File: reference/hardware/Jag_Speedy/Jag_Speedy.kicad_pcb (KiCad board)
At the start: 2 copper layers, 163 parts, among them IC1 MPX4250AP, IC10 SP720APP, IC11 VNS3NV04DP-E, IC12 SP720APP, IC2 MPX4250AP, IC3 VNS3NV04DP-E, IC4 VNS3NV04DP-E, IC5 VNS3NV04DP-E, IC6 TC4424EPA, IC7 TC4424EPA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

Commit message: Connector update
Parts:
- removed J3: Outputs02, Connector_PinHeader_1.00mm:PinHeader_2x05_P1.00mm_Horizontal
- removed J4: Power, Connector_PinHeader_1.00mm:PinHeader_1x05_P1.00mm_Horizontal
- removed J5: Bluetooth, Connector_PinHeader_1.00mm:PinHeader_1x06_P1.00mm_Horizontal
- removed J7: Canbus, Connector_PinHeader_1.00mm:PinHeader_1x06_P1.00mm_Horizontal
- J1: value Inputs -> 776087-1; footprint Connector_PinHeader_1.00mm:PinHeader_2x12_P1.00mm_Horizontal -> 776087-1:7760871
- J2: value Ouputs01 -> 776163-1; footprint Connector_PinHeader_1.00mm:PinHeader_2x07_P1.00mm_Horizontal -> 776163-1:776163-1
- moved J2 241.3 mm to (262.9, 161.3), turned to 90 degrees
- moved C23 157.9 mm to (245.1, 109.2)
- moved C24 157.9 mm to (244.8, 113.0)
- moved C25 157.9 mm to (244.8, 104.1)
- moved C26 157.9 mm to (244.8, 96.5)
- moved C27 157.9 mm to (244.8, 100.3)
- moved C28 157.9 mm to (244.8, 91.4)
- moved D1 157.9 mm to (241.0, 64.8)
- moved D10 157.9 mm to (233.7, 69.8)
- moved D11 157.9 mm to (233.7, 82.5)
- moved D12 157.9 mm to (233.7, 78.7)
- moved D13 157.9 mm to (227.3, 91.4)
- moved D14 157.9 mm to (228.3, 95.2)
- moved D15 157.9 mm to (228.3, 101.6)
- moved D16 157.9 mm to (228.3, 105.4)
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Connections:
- J1 pad 1: 3V3 -> (no net)
- J1 pad 10: O2Sensor -> PowerGnd
- J1 pad 11: PowerGnd -> 5V
- J1 pad 12: 3V3 -> (no net)
- J1 pad 13: PowerGnd -> (no net)
- J1 pad 14: CrankSensor+ -> 12V
- J1 pad 15: CrankSensor- -> CANH
- J1 pad 16: CamSensor+ -> CANL
- J1 pad 17: CamSensor- -> PowerGnd
- J1 pad 18: 5V -> PowerGnd
- J1 pad 19: FuelPressureSensor -> 5V
- J1 pad 2: CPU-D25 -> CCPump-OUT
- J1 pad 20: PowerGnd -> 3V3
- J1 pad 21: OilPressureSensor -> PowerGnd
- J1 pad 22: PowerGnd -> BluetoothRx
- J1 pad 23: ClutchSwitch -> BluetoothTx
- J1 pad 4: TPSSensor -> FuelPump-OUT
- J1 pad 5: PowerGnd -> Fan-OUT
- J1 pad 6: IATSensor -> IdlePWM-OUT
- J1 pad 7: PowerGnd -> (no net)
- J1 pad 8: CLTSensor -> Tacho-OUT
- J2 pad 1: PowerGnd -> 3V3
- J2 pad 10: Ign03-OUT -> O2Sensor
- J2 pad 11: Ign04-OUT -> PowerGnd
- J2 pad 12: Ign05-OUT -> PowerGnd
- J2 pad 13: Ign06-OUT -> PowerGnd
- J2 pad 14: PowerGnd -> CrankSensor+
- J2 pad 2: Inj01-OUT -> CPU-D25
- J2 pad 3: Inj02-OUT -> PowerGnd
- J2 pad 4: Inj03-OUT -> TPSSensor
- J2 pad 5: Inj04-OUT -> PowerGnd
- J2 pad 6: Inj05-OUT -> IATSensor
- J2 pad 7: Inj06-OUT -> PowerGnd
- J2 pad 8: Ign01-OUT -> CLTSensor
- J2 pad 9: Ign02-OUT -> PowerGnd
- U5 pad 6: Net-(J7-Pad2) -> CANL
- U5 pad 7: Net-(J7-Pad1) -> CANH

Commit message: PCB Connectors
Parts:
- moved D8 110.4 mm to (190.5, 162.6), turned to 90 degrees
- moved D2 107.0 mm to (190.5, 155.3), turned to 90 degrees
- moved D7 105.4 mm to (194.3, 162.6), turned to 90 degrees
- moved R51 105.0 mm to (190.5, 149.8), turned to 90 degrees
- moved D1 101.8 mm to (194.3, 155.3), turned to 90 degrees
- moved R39 101.4 mm to (169.8, 146.1)
- moved R45 101.4 mm to (165.4, 146.1)
- moved IC3 101.4 mm to (158.8, 148.6)
- moved IC5 101.4 mm to (158.8, 166.4)
- moved R38 101.4 mm to (166.0, 149.9)
- moved R41 101.4 mm to (166.0, 160.0)
- moved R44 101.4 mm to (169.8, 149.9)
- moved R47 101.4 mm to (166.0, 156.2)
- moved R49 101.4 mm to (166.0, 163.8)
- moved R92 101.4 mm to (138.3, 166.4)
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
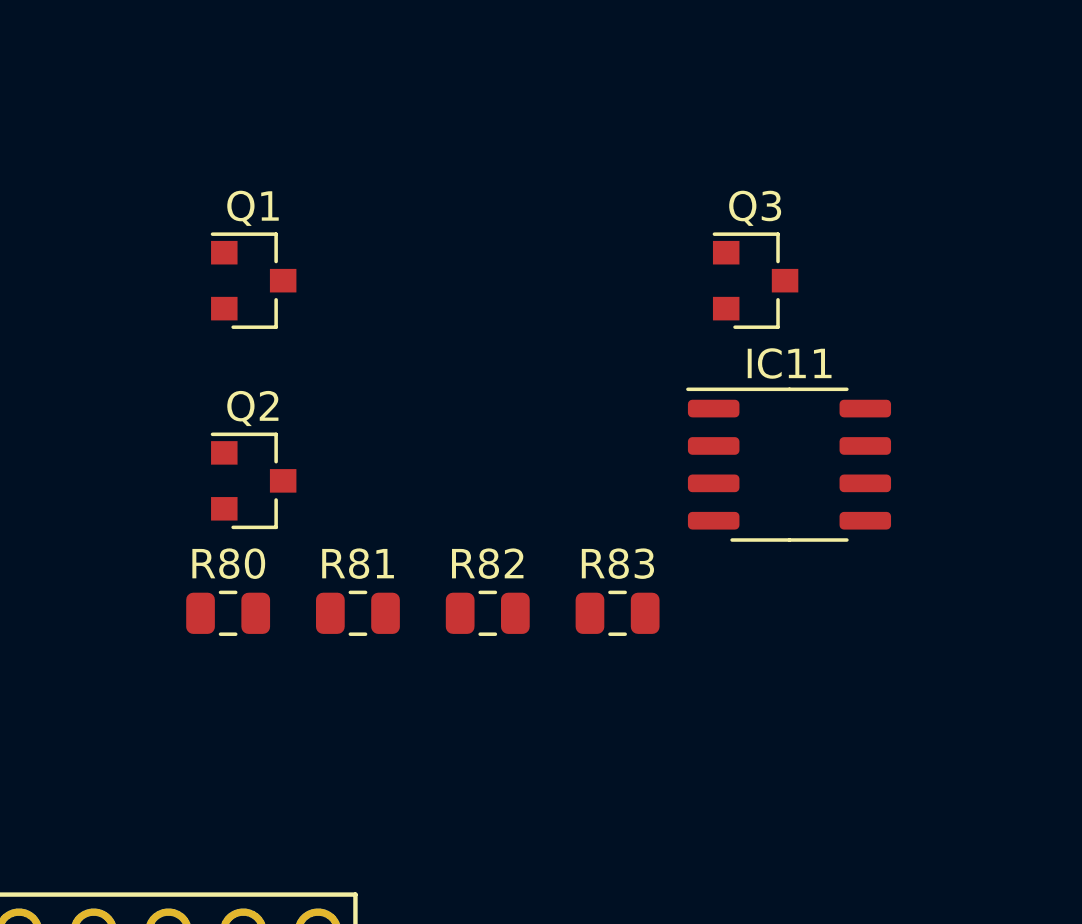
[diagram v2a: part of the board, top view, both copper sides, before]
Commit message: Added Water Pump PWM
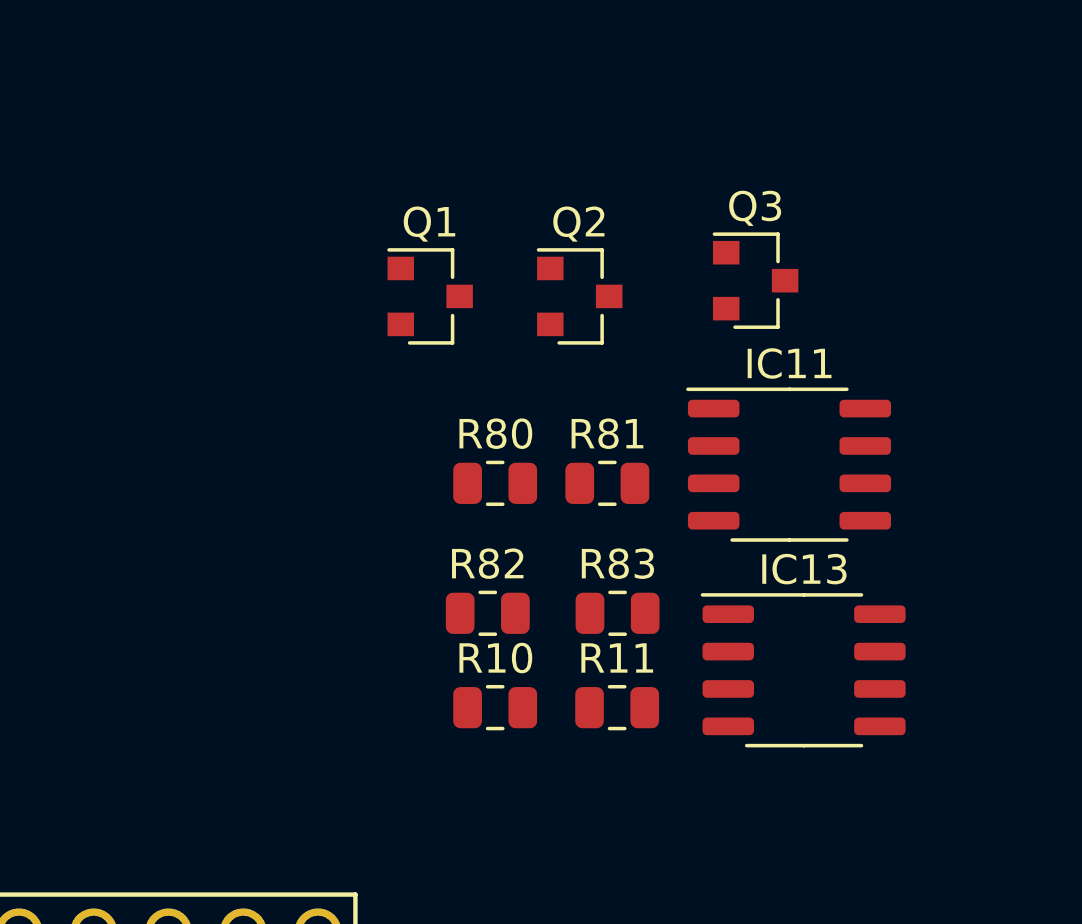
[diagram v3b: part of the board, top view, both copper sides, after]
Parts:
- added IC13: VNS3NV04DP-E, Package_SO:SO-8_3.9x4.9mm_P1.27mm, F.Cu at (228.6, 55.9)
- added R10: 100k, Resistor_SMD:R_0805_2012Metric, F.Cu at (218.1, 57.1)
- added R11: 1k, Resistor_SMD:R_0805_2012Metric, F.Cu at (222.2, 57.1)
- moved Q2 12.7 mm to (221.0, 43.2)
- moved R80 10.1 mm to (218.1, 49.5)
- moved R81 9.55 mm to (221.9, 49.5)
- moved Q1 6.02 mm to (215.9, 43.2)
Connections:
- J1 pad 12: (no net) -> WPPWM-OUT
- U3 pad 22: (no net) -> CPU-D30

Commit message: EGR Input
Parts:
- added C34: 0.1uF, Capacitor_SMD:C_0805_2012Metric, F.Cu at (244.3, 120.4)
- added C35: 0.22uF, Capacitor_SMD:C_0805_2012Metric, F.Cu at (244.3, 123.3)
- added R12: 2.49k, Resistor_SMD:R_0805_2012Metric, F.Cu at (248.7, 120.4)
- added R13: 470, Resistor_SMD:R_0805_2012Metric, F.Cu at (248.7, 123.3)
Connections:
- J2 pad 12: PowerGnd -> EGRSensor
- U3 pad 47: (no net) -> ADCClamp11

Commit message: EGT Amp
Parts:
- moved IC3 57.6 mm to (172.7, 92.7)
- moved IC5 57.6 mm to (172.7, 110.5)
- moved R38 57.6 mm to (180.0, 94.0)
- moved R39 57.6 mm to (183.8, 90.2)
- moved R41 57.6 mm to (180.0, 104.1)
- moved R44 57.6 mm to (183.8, 94.0)
- moved R45 57.6 mm to (179.4, 90.2)
- moved R47 57.6 mm to (180.0, 100.3)
- moved R49 57.6 mm to (180.0, 108.0)
- moved R92 57.6 mm to (152.3, 110.5)
- moved U5 57.6 mm to (162.0, 107.3)
- moved IC4 57.6 mm to (172.7, 101.6)
- moved R40 57.6 mm to (184.5, 105.4)
- moved R42 57.6 mm to (183.8, 113.0)
- moved R43 57.6 mm to (183.2, 109.2)
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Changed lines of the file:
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@@
   )
   (module Resistor_SMD:R_0805_2012Metric (layer F.Cu)
-    (at 169.8475 146.05)
+    (at 183.8175 90.17)
     (descr "Resistor SMD 0805 (2012 Metric), square (rectangular) end terminal, IPC_7351 nominal, (Body size source: https://docs.google.com/spreadsheets/d/1BsfQQcO9C6DZCsRaXUlFlo91Tg2WpOkGARC1WS5S8t0/edit?usp=sharing), generated with kicad-footprint-generator")
     (tags resistor)
@@
   )
   (module Package_SO:SOIC-8_3.9x4.9mm_P1.27mm (layer F.Cu)
-    (at 148.005001 163.175001)
+    (at 161.975001 107.295001)
     (descr "SOIC, 8 Pin (JEDEC MS-012AA, https://www.analog.com/media/en/package-pcb-resources/package/pkg_pdf/soic_narrow-r/r_8.pdf), generated with kicad-footprint-generator ipc_gullwing_generator.py")
     (tags "SOIC SO")
@@
   )
   (module Resistor_SMD:R_0805_2012Metric (layer F.Cu)
-    (at 138.335001 166.425001)
+    (at 152.305001 110.545001)
     (descr "Resistor SMD 0805 (2012 Metric), square (rectangular) end terminal, IPC_7351 nominal, (Body size source: https://docs.google.com/spreadsheets/d/1BsfQQcO9C6DZCsRaXUlFlo91Tg2WpOkGARC1WS5S8t0/edit?usp=sharing), generated with kicad-footprint-generator")
     (tags resistor)
@@
   )
   (module Resistor_SMD:R_0805_2012Metric (layer F.Cu)
-    (at 166.0375 163.83)
+    (at 180.0075 107.95)
     (descr "Resistor SMD 0805 (2012 Metric), square (rectangular) end terminal, IPC_7351 nominal, (Body size source: https://docs.google.com/spreadsheets/d/1BsfQQcO9C6DZCsRaXUlFlo91Tg2WpOkGARC1WS5S8t0/edit?usp=sharing), generated with kicad-footprint-generator")
     (tags resistor)
@@
   )
   (module Resistor_SMD:R_0805_2012Metric (layer F.Cu)
-    (at 166.0375 168.91)
+    (at 180.0075 113.03)
     (descr "Resistor SMD 0805 (2012 Metric), square (rectangular) end terminal, IPC_7351 nominal, (Body size source: https://docs.google.com/spreadsheets/d/1BsfQQcO9C6DZCsRaXUlFlo91Tg2WpOkGARC1WS5S8t0/edit?usp=sharing), generated with kicad-footprint-generator")
     (tags resistor)
@@
   )
   (module Resistor_SMD:R_0805_2012Metric (layer F.Cu)
-    (at 166.0375 156.21)
+    (at 180.0075 100.33)
     (descr "Resistor SMD 0805 (2012 Metric), square (rectangular) end terminal, IPC_7351 nominal, (Body size source: https://docs.google.com/spreadsheets/d/1BsfQQcO9C6DZCsRaXUlFlo91Tg2WpOkGARC1WS5S8t0/edit?usp=sharing), generated with kicad-footprint-generator")
     (tags resistor)
@@
   )
   (module Resistor_SMD:R_0805_2012Metric (layer F.Cu)
-    (at 169.8475 157.48)
+    (at 183.8175 101.6)
     (descr "Resistor SMD 0805 (2012 Metric), square (rectangular) end terminal, IPC_7351 nominal, (Body size source: https://docs.google.com/spreadsheets/d/1BsfQQcO9C6DZCsRaXUlFlo91Tg2WpOkGARC1WS5S8t0/edit?usp=sharing), generated with kicad-footprint-generator")
     (tags resistor)
@@
   )
   (module Resistor_SMD:R_0805_2012Metric (layer F.Cu)
-    (at 165.4325 146.05)
+    (at 179.4025 90.17)
     (descr "Resistor SMD 0805 (2012 Metric), square (rectangular) end terminal, IPC_7351 nominal, (Body size source: https://docs.google.com/spreadsheets/d/1BsfQQcO9C6DZCsRaXUlFlo91Tg2WpOkGARC1WS5S8t0/edit?usp=sharing), generated with kicad-footprint-generator")
     (tags resistor)
@@
   )
   (module Resistor_SMD:R_0805_2012Metric (layer F.Cu)
-    (at 169.8475 149.86)
+    (at 183.8175 93.98)
     (descr "Resistor SMD 0805 (2012 Metric), square (rectangular) end terminal, IPC_7351 nominal, (Body size source: https://docs.google.com/spreadsheets/d/1BsfQQcO9C6DZCsRaXUlFlo91Tg2WpOkGARC1WS5S8t0/edit?usp=sharing), generated with kicad-footprint-generator")
     (tags resistor)
@@
   )
   (module Resistor_SMD:R_0805_2012Metric (layer F.Cu)
-    (at 169.2425 165.1)
+    (at 183.2125 109.22)
     (descr "Resistor SMD 0805 (2012 Metric), square (rectangular) end terminal, IPC_7351 nominal, (Body size source: https://docs.google.com/spreadsheets/d/1BsfQQcO9C6DZCsRaXUlFlo91Tg2WpOkGARC1WS5S8t0/edit?usp=sharing), generated with kicad-footprint-generator")
     (tags resistor)
@@
   )
   (module Resistor_SMD:R_0805_2012Metric (layer F.Cu)
-    (at 169.8475 168.91)
+    (at 183.8175 113.03)
     (descr "Resistor SMD 0805 (2012 Metric), square (rectangular) end terminal, IPC_7351 nominal, (Body size source: https://docs.google.com/spreadsheets/d/1BsfQQcO9C6DZCsRaXUlFlo91Tg2WpOkGARC1WS5S8t0/edit?usp=sharing), generated with kicad-footprint-generator")
     (tags resistor)
@@
   )
   (module Resistor_SMD:R_0805_2012Metric (layer F.Cu)
-    (at 166.0375 160.02)
+    (at 180.0075 104.14)
     (descr "Resistor SMD 0805 (2012 Metric), square (rectangular) end terminal, IPC_7351 nominal, (Body size source: https://docs.google.com/spreadsheets/d/1BsfQQcO9C6DZCsRaXUlFlo91Tg2WpOkGARC1WS5S8t0/edit?usp=sharing), generated with kicad-footprint-generator")
     (tags resistor)
@@
   )
   (module Resistor_SMD:R_0805_2012Metric (layer F.Cu)
-    (at 170.5125 161.29)
+    (at 184.4825 105.41)
     (descr "Resistor SMD 0805 (2012 Metric), square (rectangular) end terminal, IPC_7351 nominal, (Body size source: https://docs.google.com/spreadsheets/d/1BsfQQcO9C6DZCsRaXUlFlo91Tg2WpOkGARC1WS5S8t0/edit?usp=sharing), generated with kicad-footprint-generator")
     (tags resistor)
@@
   )
   (module Resistor_SMD:R_0805_2012Metric (layer F.Cu)
-    (at 166.0375 149.86)
+    (at 180.0075 93.98)
     (descr "Resistor SMD 0805 (2012 Metric), square (rectangular) end terminal, IPC_7351 nominal, (Body size source: https://docs.google.com/spreadsheets/d/1BsfQQcO9C6DZCsRaXUlFlo91Tg2WpOkGARC1WS5S8t0/edit?usp=sharing), generated with kicad-footprint-generator")
     (tags resistor)
@@
   )
   (module Package_SO:SO-8_3.9x4.9mm_P1.27mm (layer F.Cu)
-    (at 158.75 166.37 180)
+    (at 172.72 110.49 180)
     (descr "SO, 8 Pin (https://www.nxp.com/docs/en/data-sheet/PCF8523.pdf), generated with kicad-footprint-generator ipc_gullwing_generator.py")
     (tags "SO SO")
@@
   )
   (module Package_SO:SO-8_3.9x4.9mm_P1.27mm (layer F.Cu)
-    (at 158.75 157.48 180)
+    (at 172.72 101.6 180)
     (descr "SO, 8 Pin (https://www.nxp.com/docs/en/data-sheet/PCF8523.pdf), generated with kicad-footprint-generator ipc_gullwing_generator.py")
     (tags "SO SO")
@@
   )
   (module Package_SO:SO-8_3.9x4.9mm_P1.27mm (layer F.Cu)
-    (at 158.75 148.59 180)
+    (at 172.72 92.71 180)
     (descr "SO, 8 Pin (https://www.nxp.com/docs/en/data-sheet/PCF8523.pdf), generated with kicad-footprint-generator ipc_gullwing_generator.py")
     (tags "SO SO")
